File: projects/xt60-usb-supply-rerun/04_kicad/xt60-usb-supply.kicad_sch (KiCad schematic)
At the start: 47 parts, among them J1 XT60PW-M, J2 USB-A, J3 USB-A, J4 USB-A, J5 TYPE-C-31-M-12A, Q1 AOD4185, U1 SY8368QNC, U2 SY8368QNC, U3 USBLC6-2SC6, U4 USBLC6-2SC6, U5 USBLC6-2SC6, U6 USBLC6-2SC6

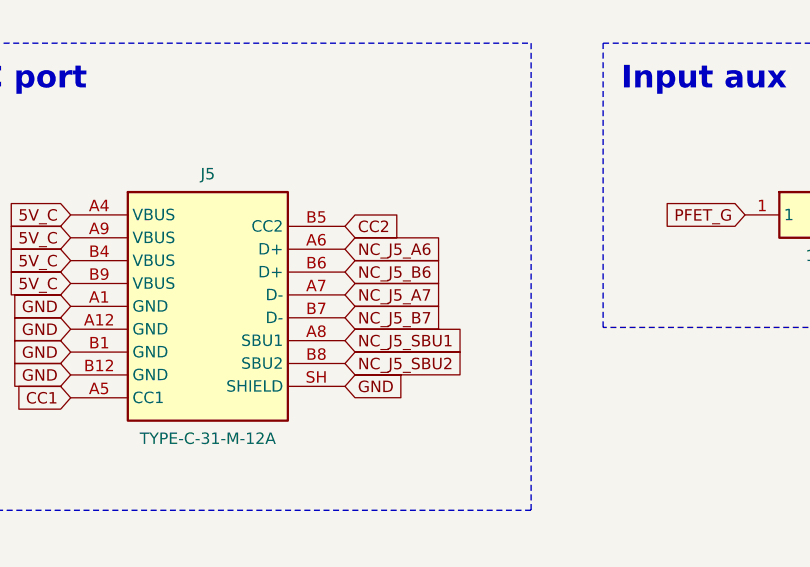
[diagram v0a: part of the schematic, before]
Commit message: xt60-usb-supply-rerun: sync through 8efa537 — review triage (USB-C DCP short ADR 0008, fab artifacts)
Co-Authored-By: Claude Fable 5 <noreply@anthropic.com>
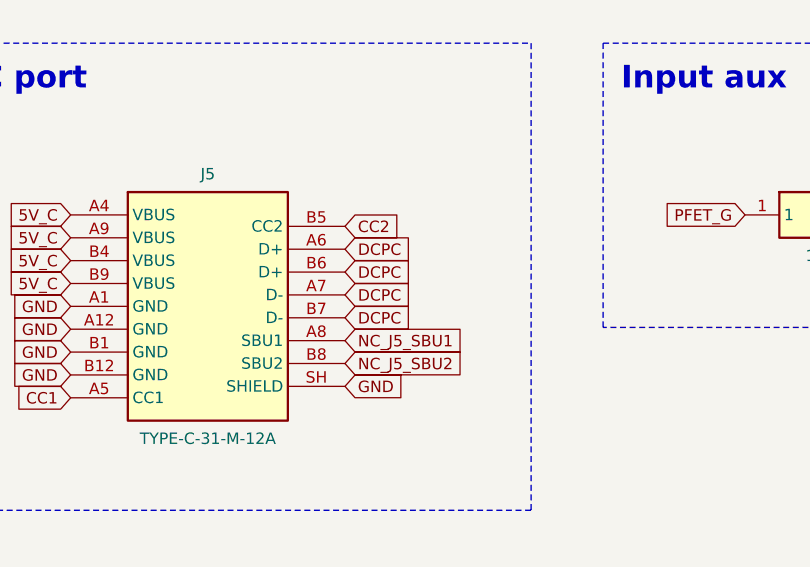
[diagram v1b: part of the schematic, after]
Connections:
- net NC_J5_A7 is gone; now on net DCPC: J5.A7 (D-)
- net NC_J5_B6 is gone; now on net DCPC: J5.B6 (D+)
- net NC_J5_B7 is gone; now on net DCPC: J5.B7 (D-)
- net NC_J5_A6 renamed DCPC
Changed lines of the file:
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@@
     (property "Intersheetrefs" "${INTERSHEETREFS}" (at 381 153.67 0) (effects (font (size 1.27 1.27)) hide))
   )
-  (global_label "NC_J5_A6" (shape input) (at 381 156.21 0) (effects (font (size 1.27 1.27)) (justify left))
+  (global_label "DCPC" (shape input) (at 381 156.21 0) (effects (font (size 1.27 1.27)) (justify left))
     (property "Intersheetrefs" "${INTERSHEETREFS}" (at 381 156.21 0) (effects (font (size 1.27 1.27)) hide))
   )
-  (global_label "NC_J5_B6" (shape input) (at 381 158.75 0) (effects (font (size 1.27 1.27)) (justify left))
+  (global_label "DCPC" (shape input) (at 381 158.75 0) (effects (font (size 1.27 1.27)) (justify left))
     (property "Intersheetrefs" "${INTERSHEETREFS}" (at 381 158.75 0) (effects (font (size 1.27 1.27)) hide))
   )
-  (global_label "NC_J5_A7" (shape input) (at 381 161.29 0) (effects (font (size 1.27 1.27)) (justify left))
+  (global_label "DCPC" (shape input) (at 381 161.29 0) (effects (font (size 1.27 1.27)) (justify left))
     (property "Intersheetrefs" "${INTERSHEETREFS}" (at 381 161.29 0) (effects (font (size 1.27 1.27)) hide))
   )
-  (global_label "NC_J5_B7" (shape input) (at 381 163.83 0) (effects (font (size 1.27 1.27)) (justify left))
+  (global_label "DCPC" (shape input) (at 381 163.83 0) (effects (font (size 1.27 1.27)) (justify left))
     (property "Intersheetrefs" "${INTERSHEETREFS}" (at 381 163.83 0) (effects (font (size 1.27 1.27)) hide))
   )
